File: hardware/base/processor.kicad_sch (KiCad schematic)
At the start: 14 parts, among them J4 Debug UART, SW1 RESET, SW2 BOOT, SW4 NAV, U1 PI4IOE5V9554A, U3 ESP32-S3-WROOM-1-PinOrder

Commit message: layout
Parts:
- added R3, R4: 4.7k, Resistor_SMD:R_0402_1005Metric, symbol Device:R_Small
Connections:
- net AUX_REG_EN: now also U1.10 (P5); no longer U1.11 (P6)
- net GPS_FIX: now also U1.4 (P0); no longer U1.6 (P2)
- net GPS_FORCE_ON: now also U1.5 (P1); no longer U1.7 (P3)
- net ISENSE_INT: now also U1.12 (P7); no longer U1.10 (P5)
- net NAV_BTN: now also U1.7 (P3); no longer U1.5 (P1)
- net SHUTDOWN: now also U1.11 (P6); no longer U1.12 (P7)
- net STATUS_IOEXP0: now also U1.6 (P2); no longer U1.4 (P0)
- net SYS_I2C.SCL: now also U1.15 (SDA), U3.34 (MTDI/GPIO41/CLK_OUT1), R4.2; no longer U1.14 (SCL), U3.33 (MTDO/GPIO40/CLK_OUT2)
- net SYS_I2C.SDA: now also U1.14 (SCL), U3.33 (MTDO/GPIO40/CLK_OUT2), R3.2; no longer U1.15 (SDA), U3.34 (MTDI/GPIO41/CLK_OUT1)
- net exp_led: now reaches D7.2 (A), R2.1
- net esp_led: now reaches D6.2 (A), R41.1
- new net VDD_AUX_3V3: R3.1, R4.1
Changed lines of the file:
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@@
   (junction (at 85.09 154.94) (diameter 0) (color 0 0 0 0)
   )
+  (junction (at 222.25 63.5) (diameter 0) (color 0 0 0 0)
+  )
+  (junction (at 62.23 106.68) (diameter 0) (color 0 0 0 0)
+  )
   (junction (at 195.58 72.39) (diameter 0) (color 0 0 0 0)
   )
-  (junction (at 62.23 106.68) (diameter 0) (color 0 0 0 0)
+  (junction (at 198.12 74.93) (diameter 0) (color 0 0 0 0)
+  )
+  (junction (at 222.25 72.39) (diameter 0) (color 0 0 0 0)
   )
   (junction (at 229.87 96.52) (diameter 0) (color 0 0 0 0)
@@
   (junction (at 184.15 104.14) (diameter 0) (color 0 0 0 0)
   )
-  (junction (at 198.12 74.93) (diameter 0) (color 0 0 0 0)
-  )
   (junction (at 39.37 49.53) (diameter 0) (color 0 0 0 0)
   )
   (junction (at 229.87 90.17) (diameter 0) (color 0 0 0 0)
+  )
+  (junction (at 227.33 74.93) (diameter 0) (color 0 0 0 0)
   )
   (no_connect (at 182.88 63.5))
@@
     (stroke (width 0) (type default) (color 0 0 0 0))
   )
-  (wire (pts (xy 254 80.01) (xy 251.46 80.01))
+  (wire (pts (xy 254 74.93) (xy 251.46 74.93))
     (stroke (width 0) (type default) (color 0 0 0 0))
   )
@@
     (stroke (width 0) (type default) (color 0 0 0 0))
   )
-  (wire (pts (xy 262.89 72.39) (xy 251.46 72.39))
+  (wire (pts (xy 262.89 77.47) (xy 251.46 77.47))
     (stroke (width 0) (type default) (color 0 0 0 0))
   )
@@
     (stroke (width 0) (type default) (color 0 0 0 0))
   )
+  (wire (pts (xy 227.33 74.93) (xy 231.14 74.93))
+    (stroke (width 0) (type default) (color 0 0 0 0))
+  )
   (wire (pts (xy 52.07 82.55) (xy 64.77 82.55))
     (stroke (width 0) (type default) (color 0 0 0 0))
@@
     (stroke (width 0) (type default) (color 0 0 0 0))
   )
-  (wire (pts (xy 254 90.17) (xy 251.46 90.17))
+  (wire (pts (xy 198.12 74.93) (xy 227.33 74.93))
+    (stroke (width 0) (type default) (color 0 0 0 0))
+  )
+  (wire (pts (xy 254 85.09) (xy 251.46 85.09))
     (stroke (width 0) (type default) (color 0 0 0 0))
   )
@@
     (stroke (width 0) (type default) (color 0 0 0 0))
   )
+  (wire (pts (xy 222.25 72.39) (xy 231.14 72.39))
+    (stroke (width 0) (type default) (color 0 0 0 0))
+  )
   (wire (pts (xy 39.37 49.53) (xy 64.77 49.53))
     (stroke (width 0) (type default) (color 0 0 0 0))
@@
     (stroke (width 0) (type default) (color 0 0 0 0))
   )
+  (wire (pts (xy 227.33 69.85) (xy 227.33 74.93))
+    (stroke (width 0) (type default) (color 0 0 0 0))
+  )
   (wire (pts (xy 186.055 69.85) (xy 182.88 69.85))
     (stroke (width 0) (type default) (color 0 0 0 0))
@@
     (stroke (width 0) (type default) (color 0 0 0 0))
   )
-  (wire (pts (xy 251.46 74.93) (xy 262.89 74.93))
+  (wire (pts (xy 251.46 80.01) (xy 262.89 80.01))
     (stroke (width 0) (type default) (color 0 0 0 0))
   )
@@
     (stroke (width 0) (type default) (color 0 0 0 0))
   )
+  (wire (pts (xy 222.25 63.5) (xy 222.25 64.77))
+    (stroke (width 0) (type default) (color 0 0 0 0))
+  )
   (bus (pts (xy 49.53 90.17) (xy 49.53 92.71))
     (stroke (width 0) (type default) (color 0 0 0 0))
@@
     (stroke (width 0) (type default) (color 0 0 0 0))
   )
+  (wire (pts (xy 222.25 62.23) (xy 222.25 63.5))
+    (stroke (width 0) (type default) (color 0 0 0 0))
+  )
   (wire (pts (xy 140.97 158.75) (xy 139.7 158.75))
     (stroke (width 0) (type default) (color 0 0 0 0))
@@
     (stroke (width 0) (type default) (color 0 0 0 0))
   )
+  (wire (pts (xy 222.25 69.85) (xy 222.25 72.39))
+    (stroke (width 0) (type default) (color 0 0 0 0))
+  )
   (bus (pts (xy 49.53 82.55) (xy 49.53 80.01))
     (stroke (width 0) (type default) (color 0 0 0 0))
@@
     (stroke (width 0) (type default) (color 0 0 0 0))
   )
-  (wire (pts (xy 251.46 85.09) (xy 254 85.09))
-    (stroke (width 0) (type default) (color 0 0 0 0))
-  )
-  (wire (pts (xy 195.58 72.39) (xy 231.14 72.39))
+  (wire (pts (xy 251.46 90.17) (xy 254 90.17))
+    (stroke (width 0) (type default) (color 0 0 0 0))
+  )
+  (wire (pts (xy 227.33 64.77) (xy 227.33 63.5))
     (stroke (width 0) (type default) (color 0 0 0 0))
   )
@@
     (stroke (width 0) (type default) (color 0 0 0 0))
   )
+  (wire (pts (xy 222.25 63.5) (xy 227.33 63.5))
+    (stroke (width 0) (type default) (color 0 0 0 0))
+  )
   (wire (pts (xy 229.87 87.63) (xy 231.14 87.63))
     (stroke (width 0) (type default) (color 0 0 0 0))
   )
-  (wire (pts (xy 198.12 74.93) (xy 231.14 74.93))
-    (stroke (width 0) (type default) (color 0 0 0 0))
-  )
   (wire (pts (xy 52.07 67.31) (xy 64.77 67.31))
     (stroke (width 0) (type default) (color 0 0 0 0))
@@
     (stroke (width 0) (type default) (color 0 0 0 0))
   )
-  (wire (pts (xy 254 77.47) (xy 251.46 77.47))
+  (wire (pts (xy 254 72.39) (xy 251.46 72.39))
     (stroke (width 0) (type default) (color 0 0 0 0))
   )
@@
     (stroke (width 0) (type default) (color 0 0 0 0))
   )
+  (wire (pts (xy 195.58 72.39) (xy 222.25 72.39))
+    (stroke (width 0) (type default) (color 0 0 0 0))
+  )
   (wire (pts (xy 229.87 90.17) (xy 229.87 87.63))
     (stroke (width 0) (type default) (color 0 0 0 0))
@@
     (effects (font (size 0.8 0.8)) (justify left bottom))
   )
-  (label "STATUS_IOEXP0" (at 262.89 72.39 180)
+  (label "STATUS_IOEXP0" (at 262.89 77.47 180)
     (effects (font (size 0.8 0.8)) (justify right bottom))
   )
@@
     (effects (font (size 0.8 0.8)) (justify left bottom))
   )
-  (label "SYS_I2C.SCL" (at 193.04 72.39 180)
+  (label "SYS_I2C.SCL" (at 193.04 74.93 180)
     (effects (font (size 0.8 0.8)) (justify right bottom))
   )
@@
     (effects (font (size 0.8 0.8)) (justify left bottom))
   )
+  (label "exp_led" (at 133.35 158.75 0)
+    (effects (font (size 0.8 0.8)) (justify left bottom))
+  )
   (label "SDMMC.D2" (at 192.405 49.53 180)
     (effects (font (size 0.8 0.8)) (justify right bottom))
@@
     (effects (font (size 0.8 0.8)) (justify left bottom))
   )
+  (label "esp_led" (at 133.35 144.78 0)
+    (effects (font (size 0.8 0.8)) (justify left bottom))
+  )
   (label "STATUS_ESP" (at 52.07 74.93 0)
     (effects (font (size 0.8 0.8)) (justify left bottom))
@@
     (effects (font (size 0.8 0.8)) (justify left bottom))
   )
-  (label "SYS_I2C.SDA" (at 193.04 74.93 180)
+  (label "SYS_I2C.SDA" (at 193.04 72.39 180)
     (effects (font (size 0.8 0.8)) (justify right bottom))
   )
@@
     (effects (font (size 0.8 0.8)) (justify left bottom))
   )
-  (label "NAV_BTN" (at 262.89 74.93 180)
+  (label "NAV_BTN" (at 262.89 80.01 180)
     (effects (font (size 0.8 0.8)) (justify right bottom))
   )
@@
     (effects (font (size 0.8 0.8)) (justify right))
   )
-  (hierarchical_label "ISENSE_INT" (shape input) (at 254 85.09 0)
+  (hierarchical_label "ISENSE_INT" (shape input) (at 254 90.17 0)
     (effects (font (size 0.8 0.8)) (justify left))
   )
@@
     (effects (font (size 0.8 0.8)) (justify right))
   )
-  (hierarchical_label "GPS_FORCE_ON" (shape output) (at 254 80.01 0)
+  (hierarchical_label "GPS_FORCE_ON" (shape output) (at 254 74.93 0)
     (effects (font (size 0.8 0.8)) (justify left))
   )
@@
     (effects (font (size 0.8 0.8)) (justify right))
   )
-  (hierarchical_label "GPS_FIX" (shape input) (at 254 77.47 0)
+  (hierarchical_label "GPS_FIX" (shape input) (at 254 72.39 0)
     (effects (font (size 0.8 0.8)) (justify left))
   )
-  (hierarchical_label "SHUTDOWN" (shape output) (at 254 90.17 0)
+  (hierarchical_label "SHUTDOWN" (shape output) (at 254 87.63 0)
     (effects (font (size 0.8 0.8)) (justify left))
   )
@@
     (effects (font (size 0.8 0.8)) (justify left))
   )
-  (hierarchical_label "AUX_REG_EN" (shape output) (at 254 87.63 0)
+  (hierarchical_label "AUX_REG_EN" (shape output) (at 254 85.09 0)
     (effects (font (size 0.8 0.8)) (justify left))
   )
@@
     (pin "2")
   )
+  (symbol (lib_id "Device:R_Small") (at 227.33 67.31 0) (unit 1)
+    (in_bom yes) (on_board yes)
+    (property "Reference" "R4" (id 0) (at 228.6 66.04 0)
+      (effects (font (size 0.8 0.8)) (justify left))
+    )
+    (property "Value" "4.7k" (id 1) (at 228.6 67.31 0)
+      (effects (font (size 0.8 0.8)) (justify left))
+    )
+    (property "Footprint" "Resistor_SMD:R_0402_1005Metric" (id 2) (at 227.33 67.31 0)
+      (effects (font (size 0.8 0.8)) hide)
+    )
+    (property "Datasheet" "~" (id 3) (at 227.33 67.31 0)
+      (effects (font (size 0.8 0.8)) hide)
+    )
+    (pin "1")
+    (pin "2")
+  )
   (symbol (lib_id "Device:R_Small") (at 39.37 45.72 0) (mirror y) (unit 1)
     (in_bom yes) (on_board yes)
@@
     (pin "1")
     (pin "2")
+  )
+  (symbol (lib_id "bt_power:VDD_AUX_3V3") (at 222.25 62.23 0) (unit 1)
+    (in_bom no) (on_board no) (fields_autoplaced)
+    (property "Reference" "#PWR0142" (id 0) (at 222.7834 62.23 0)
+      (effects (font (size 1.27 1.27)) hide)
+    )
+    (property "Value" "VDD_AUX_3V3" (id 1) (at 222.25 58.42 0)
+      (effects (font (size 0.8 0.8)))
+    )
+    (property "Footprint" "" (id 2) (at 222.7834 62.23 0)
+      (effects (font (size 1.27 1.27)) hide)
+    )
+    (property "Datasheet" "" (id 3) (at 222.7834 62.23 0)
+      (effects (font (size 1.27 1.27)) hide)
+    )
+    (pin "1")
   )
   (symbol (lib_id "power:GND") (at 184.15 114.3 0) (mirror y) (unit 1)
@@
       (effects (font (size 0.8 0.8)) hide)
     )
+    (pin "1")
+    (pin "2")
+  )
+  (symbol (lib_id "Device:R_Small") (at 222.25 67.31 0) (unit 1)
+    (in_bom yes) (on_board yes)
+    (property "Reference" "R3" (id 0) (at 223.52 66.04 0)
+      (effects (font (size 0.8 0.8)) (justify left))
+    )
+    (property "Value" "4.7k" (id 1) (at 223.52 67.31 0)
+      (effects (font (size 0.8 0.8)) (justify left))
+    )
+    (property "Footprint" "Resistor_SMD:R_0402_1005Metric" (id 2) (at 222.25 67.31 0)
+      (effects (font (size 0.8 0.8)) hide)
+    )
+    (property "Datasheet" "~" (id 3) (at 222.25 67.31 0)
+      (effects (font (size 0.8 0.8)) hide)
+    )

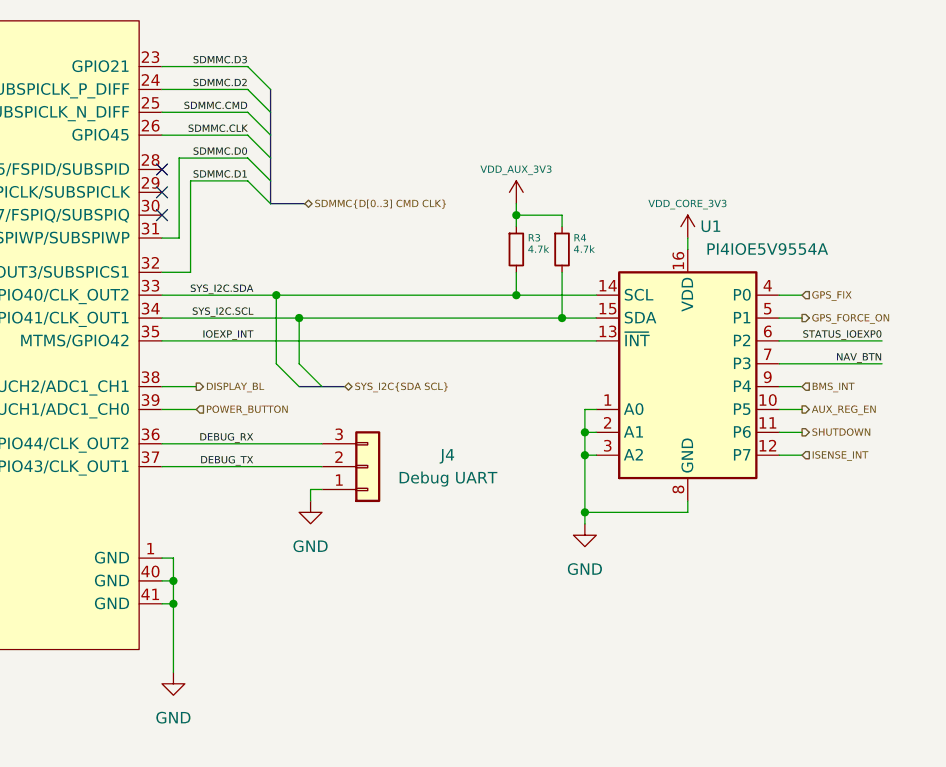
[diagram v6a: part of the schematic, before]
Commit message: more layout, optimising i2c
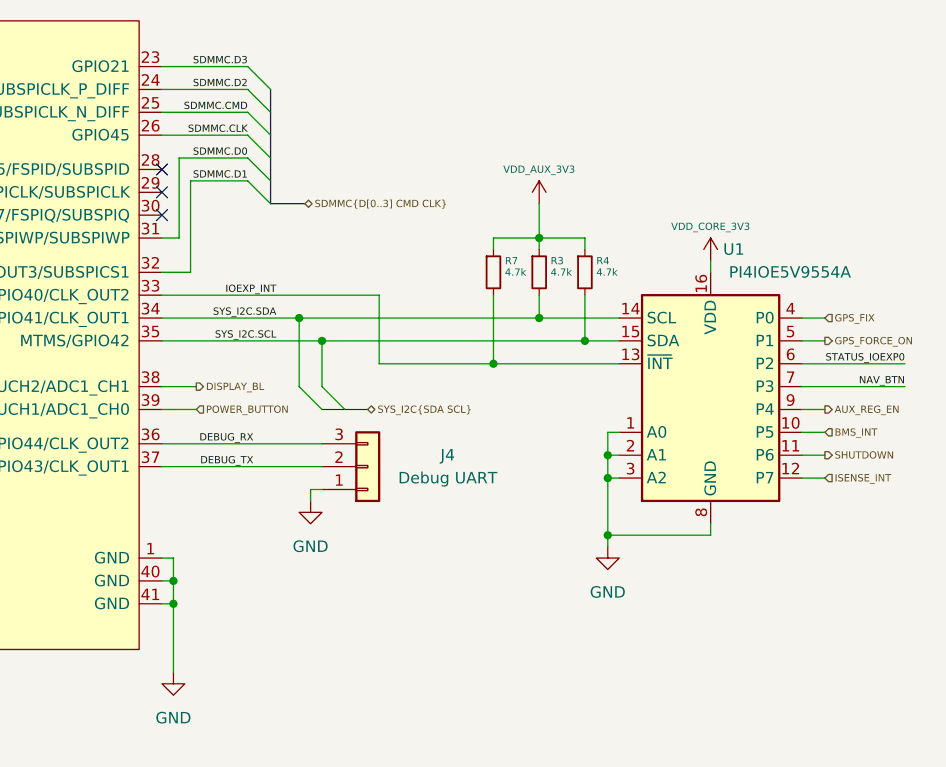
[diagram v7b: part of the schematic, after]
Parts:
- added R7: 4.7k, Resistor_SMD:R_0402_1005Metric, symbol Device:R_Small
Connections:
- net AUX_REG_EN: now also U1.9 (P4); no longer U1.10 (P5)
- net BMS_INT: now also U1.10 (P5); no longer U1.9 (P4)
- net IOEXP_INT: now also U3.33 (MTDO/GPIO40/CLK_OUT2), R7.2; no longer U3.35 (MTMS/GPIO42)
- net SYS_I2C.SCL: now also U3.35 (MTMS/GPIO42); no longer U3.34 (MTDI/GPIO41/CLK_OUT1)
- net SYS_I2C.SDA: now also U3.34 (MTDI/GPIO41/CLK_OUT1); no longer U3.33 (MTDO/GPIO40/CLK_OUT2)
- net VDD_AUX_3V3: now also R7.1
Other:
- moved on the sheet: R3, R4, U1

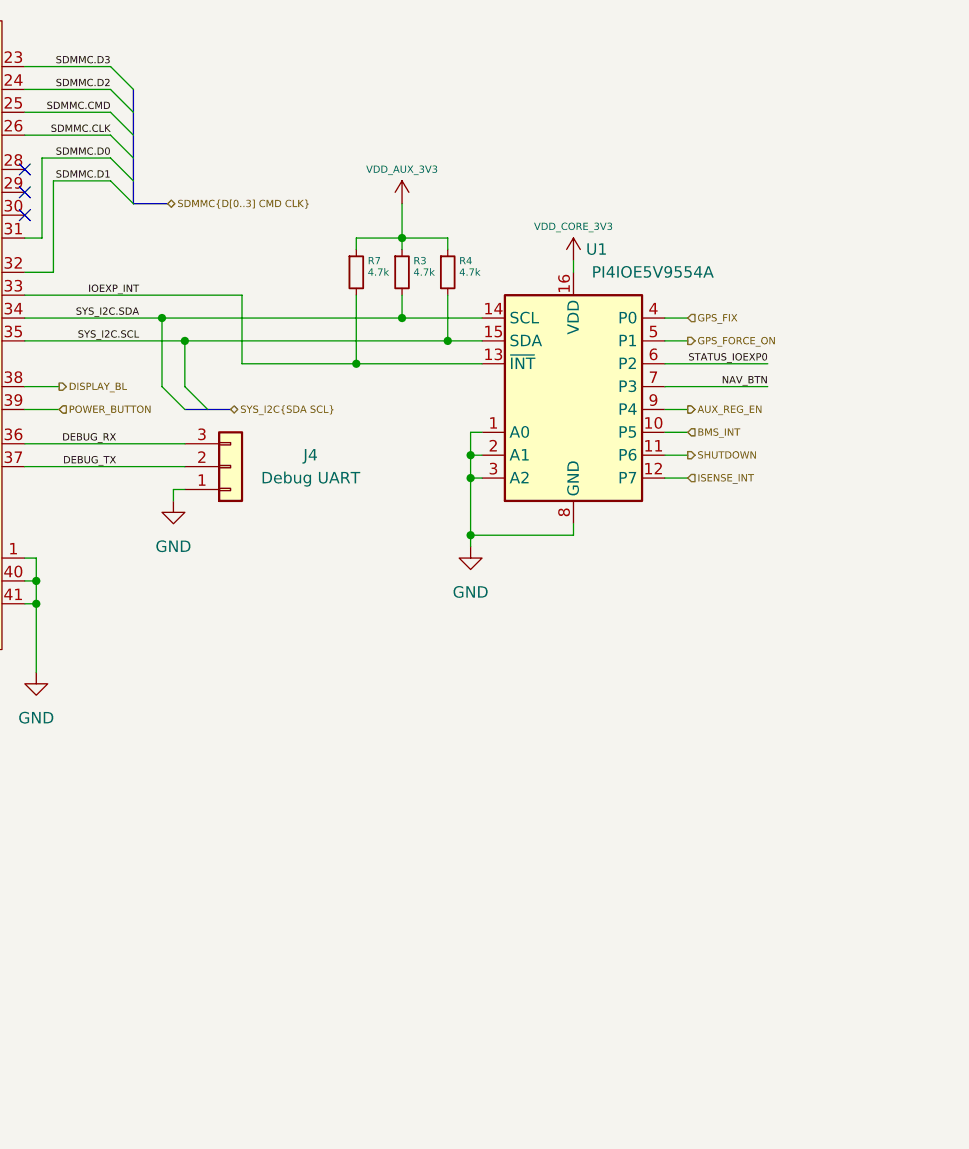
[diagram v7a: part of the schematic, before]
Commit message: layout complete, drc checks and tweaks to silkscreen, attempting geo reannotate
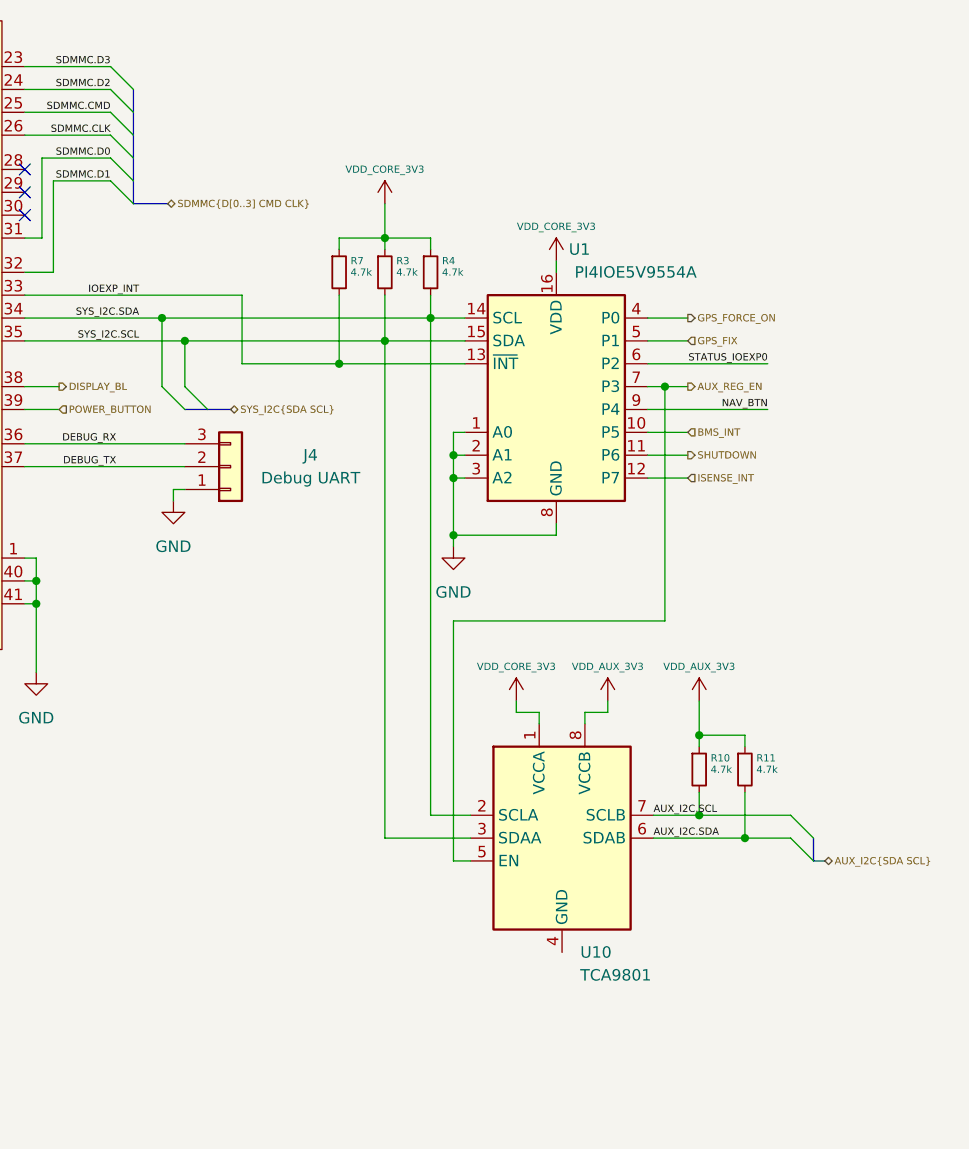
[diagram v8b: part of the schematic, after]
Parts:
- added R10, R11: 4.7k, Resistor_SMD:R_0402_1005Metric, symbol Device:R_Small
- added U10: TCA9801, Package_SO:VSSOP-8_3.0x3.0mm_P0.65mm, symbol Interface:TCA9801
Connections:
- net AUX_REG_EN: now also U1.7 (P3), U10.5 (EN); no longer U1.9 (P4)
- net GPS_FIX: now also U1.5 (P1); no longer U1.4 (P0)
- net GPS_FORCE_ON: now also U1.4 (P0); no longer U1.5 (P1)
- net NAV_BTN: now also U1.9 (P4); no longer U1.7 (P3)
- net SYS_I2C.SCL: now also R3.2, U10.3 (SDAA); no longer R4.2
- net SYS_I2C.SDA: now also R4.2, U10.2 (SCLA); no longer R3.2
- net VDD_AUX_3V3: now also R10.1, R11.1, U10.8 (VCCB); no longer R3.1, R4.1, R7.1
- net VDD_CORE_3V3: now also R3.1, R4.1, R7.1, U10.1 (VCCA)
- new net AUX_I2C.SCL: R10.2, U10.7 (SCLB)
- new net AUX_I2C.SDA: R11.2, U10.6 (SDAB)
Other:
- moved on the sheet: R7, U1
